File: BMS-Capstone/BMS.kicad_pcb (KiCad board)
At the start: 2 copper layers, 1 part, among them IC1 MP2634

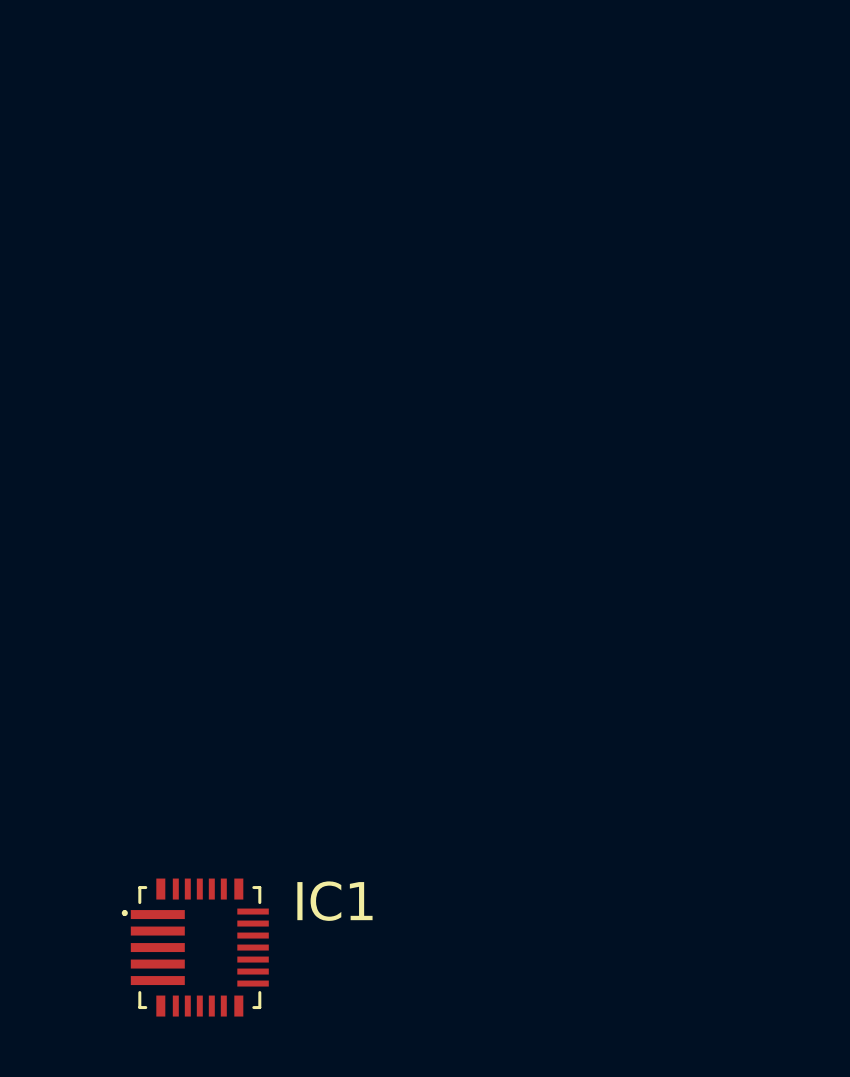
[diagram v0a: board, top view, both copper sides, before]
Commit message: Designed one entire MP chip layout
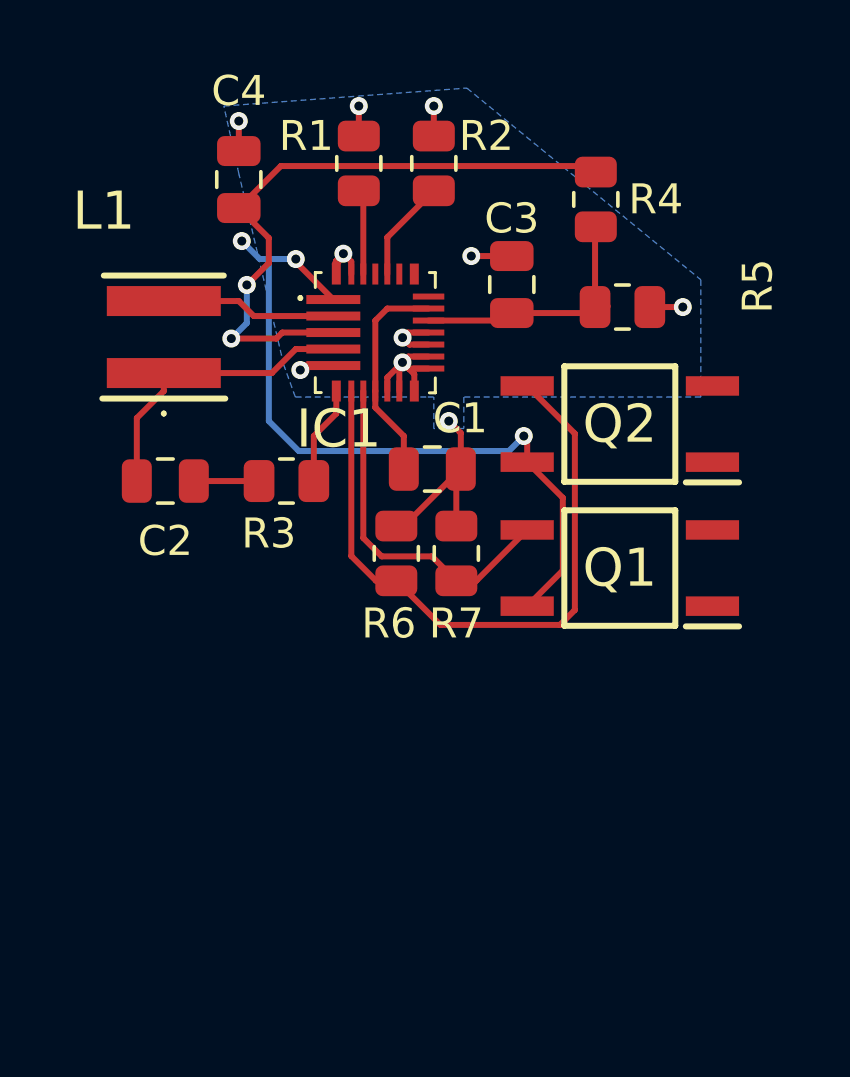
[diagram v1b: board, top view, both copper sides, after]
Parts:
- added C1: C, Capacitor_SMD:C_0805_2012Metric, F.Cu at (157.4, 79.1)
- added C2: C, Capacitor_SMD:C_0805_2012Metric, F.Cu at (148.6, 79.5)
- added C3: C, Capacitor_SMD:C_0805_2012Metric, F.Cu at (160.1, 73.0)
- added C4: C, Capacitor_SMD:C_0805_2012Metric, F.Cu at (151.0, 69.5)
- added L1: L, SamacSys_Parts:MPLAL4020R47 Inductor, F.Cu at (148.5, 74.7)
- added Q1: FODM121, SamacSys_Parts:SOP254P675X240-4N, F.Cu at (163.7, 82.4)
- added Q2: FODM121, SamacSys_Parts:SOP254P675X240-4N, F.Cu at (163.7, 77.6)
- added R1: R, Resistor_SMD:R_0805_2012Metric, F.Cu at (155.0, 68.9)
- added R2: R, Resistor_SMD:R_0805_2012Metric, F.Cu at (157.5, 68.9)
- added R3: 0, Resistor_SMD:R_0805_2012Metric, F.Cu at (152.6, 79.5)
- added R4: R, Resistor_SMD:R_0805_2012Metric, F.Cu at (162.9, 70.1)
- added R5: R, Resistor_SMD:R_0805_2012Metric, F.Cu at (163.8, 73.7)
- added R6: R, Resistor_SMD:R_0805_2012Metric, F.Cu at (156.2, 81.9)
- added R7: R, Resistor_SMD:R_0805_2012Metric, F.Cu at (158.2, 81.9)
- IC1: value MP2634 -> MP2643; footprint SamacSys_Parts:MP2634 -> SamacSys_Parts:MP2639AGRZ
- moved IC1 21.3 mm to (155.6, 74.5)
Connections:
- IC1 pad 1: unconnected-(IC1-CL-Pad1) -> /BMS Board/CELL1+/CELL2-
- IC1 pad 10: unconnected-(IC1-AGND-Pad10) -> /BMS Board/CELL1-
- IC1 pad 11: unconnected-(IC1-AGND-Pad11) -> /BMS Board/CELL1-
- IC1 pad 12: unconnected-(IC1-AGND-Pad12) -> /BMS Board/CELL1-
- IC1 pad 13: unconnected-(IC1-AGND-Pad13) -> /BMS Board/CELL1-
- IC1 pad 14: unconnected-(IC1-AGND-Pad14) -> /BMS Board/CELL1-
- IC1 pad 15: unconnected-(IC1-AGND-Pad15) -> /BMS Board/CELL1-
- IC1 pad 16: unconnected-(IC1-AGND-Pad16) -> /BMS Board/CELL1-
- IC1 pad 17: unconnected-(IC1-CU_FB-Pad17) -> Net-(IC1-CU_FB)
- IC1 pad 18: unconnected-(IC1-LOGIC-Pad18) -> /BMS Board/VCC1
- IC1 pad 2: unconnected-(IC1-LX-Pad2) -> Net-(IC1-LX)
- IC1 pad 22: unconnected-(IC1-LBC-Pad22) -> Net-(IC1-LBC)
- IC1 pad 23: unconnected-(IC1-AGND-Pad23) -> /BMS Board/CELL1-
- IC1 pad 24: unconnected-(IC1-UBC-Pad24) -> Net-(IC1-UBC)
- IC1 pad 25: unconnected-(IC1-AGND-Pad25) -> /BMS Board/CELL1-
- IC1 pad 26: unconnected-(IC1-AGND-Pad26) -> /BMS Board/CELL1-
- IC1 pad 3: unconnected-(IC1-CU-Pad3) -> /BMS Board/CELL2+/CELL3-
- IC1 pad 4: unconnected-(IC1-SW-Pad4) -> Net-(IC1-SW)
- IC1 pad 5: unconnected-(IC1-PGND-Pad5) -> /BMS Board/CELL1-
- IC1 pad 6: unconnected-(IC1-BST-Pad6) -> Net-(IC1-BST)
- IC1 pad 7: unconnected-(IC1-EN-Pad7) -> Net-(IC1-EN)
- IC1 pad 8: unconnected-(IC1-MODE-Pad8) -> Net-(IC1-MODE)
- IC1 pad 9: unconnected-(IC1-4V5-Pad9) -> /BMS Board/VCC1
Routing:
- net /BMS Board/CELL1+/CELL2-: track 0.00 -> 25.1 mm, vias 0 -> 3
- net Net-(IC1-EN): track 0.00 -> 22.2 mm
- net /BMS Board/CELL1-: track 0.00 -> 22.2 mm, vias 0 -> 10
- net /BMS Board/CELL2+/CELL3-: track 0.00 -> 21.7 mm, vias 0 -> 2
- net Net-(IC1-MODE): track 0.00 -> 11.9 mm
- net Net-(IC1-SW): track 0.00 -> 9.95 mm
- net Net-(IC1-CU_FB): track 0.00 -> 8.67 mm
- net /BMS Board/VCC1: track 0.00 -> 7.28 mm
- net Net-(IC1-LX): track 0.00 -> 5.86 mm
- net Net-(IC1-LBC): track 0.00 -> 3.42 mm
- net Net-(IC1-BST): track 0.00 -> 3.31 mm
- net Net-(IC1-UBC): track 0.00 -> 2.84 mm
- net Net-(C2-Pad1): track 0.00 -> 2.18 mm
- added copper zone on B.Cu, net /BMS Board/CELL1-

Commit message: Fixes
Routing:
- net /BMS Board/CELL1-: track 22.2 -> 24.9 mm, vias 10 -> 11
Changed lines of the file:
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@@
 		(tags "resistor")
 		(property "Reference" "R5"
-			(at 4.5125 -0.7 90)
+			(at 2.7125 -1.2 180)
 			(layer "F.SilkS")
 			(effects
@@
 	)
 	(segment
+		(start 155.55 72.6)
+		(end 155.55 70.834429)
+		(width 0.2)
+		(layer "F.Cu")
+		(net 5)
+	)
+	(segment
 		(start 160.1 72)
 		(end 158.75 72)
@@
 		(start 154.75 72.186915)
 		(end 154.484992 71.921907)
+		(width 0.2)
+		(layer "F.Cu")
+		(net 5)
+	)
+	(segment
+		(start 155.55 70.834429)
+		(end 156.226266 70.158163)
 		(width 0.2)
 		(layer "F.Cu")
@@
 		(net 5)
 	)
+	(via
+		(at 156.226266 70.158163)
+		(size 0.6)
+		(drill 0.3)
+		(layers "F.Cu" "B.Cu")
+		(free yes)
+		(net 5)
+	)

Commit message: More fixes
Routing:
- net /BMS Board/CELL1-: track 24.9 -> 23.0 mm
- net /BMS Board/CELL1+/CELL2-: track 25.1 -> 26.0 mm

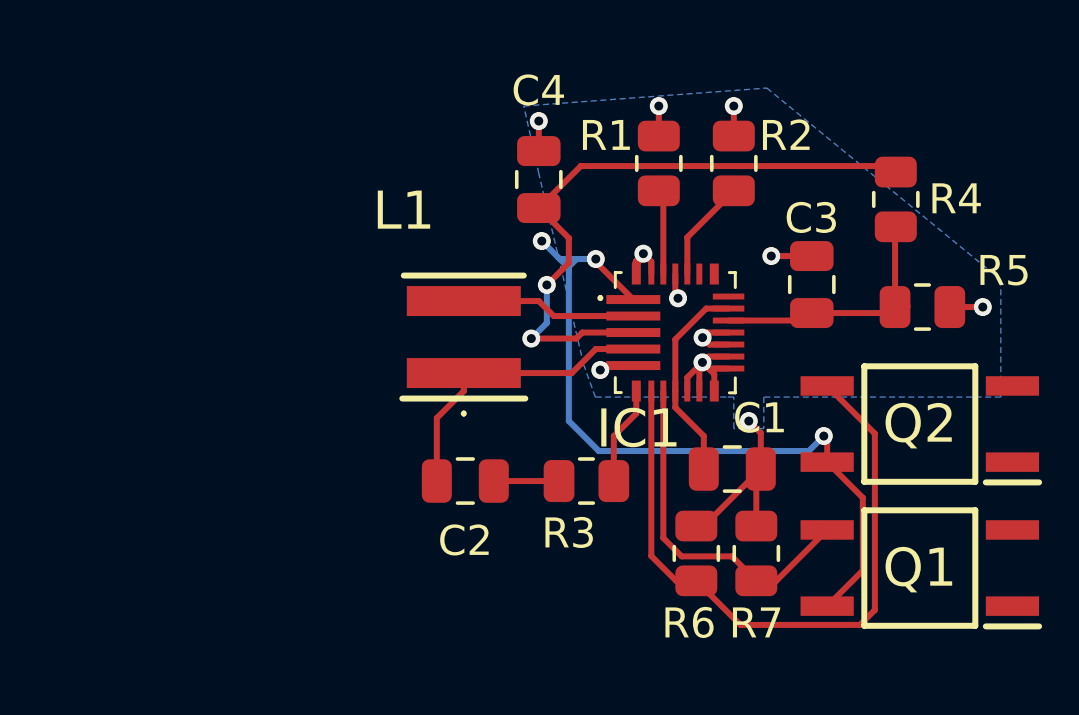
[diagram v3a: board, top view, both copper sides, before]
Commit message: added CL capacitor
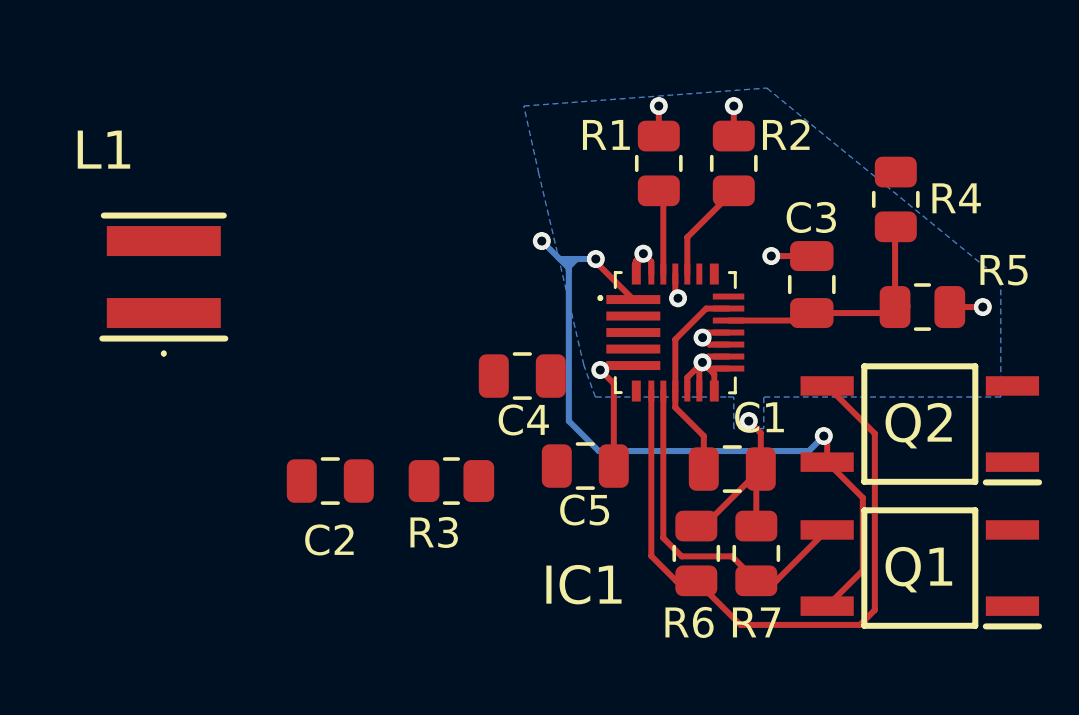
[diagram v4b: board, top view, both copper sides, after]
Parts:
- added C5: C, Capacitor_SMD:C_0805_2012Metric, F.Cu at (152.6, 79.0)
- moved L1 10.2 mm to (138.5, 72.7)
- moved C4 6.57 mm to (150.4, 76.0), turned to 0 degrees
- moved C2 4.50 mm to (144.1, 79.5)
- moved R3 4.50 mm to (148.1, 79.5)
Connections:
- net /BMS Board/CELL1+/CELL2- renamed /BMS Board/1Lower
- net /BMS Board/CELL1- renamed /BMS Board/1GND
- net /BMS Board/CELL2+/CELL3- renamed /BMS Board/1Upper
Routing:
- net /BMS Board/1Upper: track 21.7 -> 0.35 mm, vias 2 -> 0
- net Net-(IC1-SW): track 9.95 -> 0.00 mm
- net Net-(IC1-LX): track 5.86 -> 0.00 mm
- net Net-(IC1-BST): track 3.31 -> 0.00 mm
- net /BMS Board/1GND: track 23.0 -> 25.4 mm, vias 11 -> 10
- net Net-(C2-Pad1): track 2.18 -> 0.00 mm

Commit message: Redid the whole thing
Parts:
- moved R4 12.1 mm to (158.5, 81.4), turned to 90 degrees
- moved C3 7.78 mm to (156.5, 79.8), turned to 90 degrees
- moved L1 7.56 mm to (145.6, 75.3), turned to 0 degrees
- moved Q2 7.16 mm to (164.6, 84.7)
- moved R5 6.81 mm to (158.5, 78.0), turned to 90 degrees
- moved C2 5.69 mm to (148.0, 83.6), turned to 90 degrees
- moved C1 5.45 mm to (153.7, 83.0)
- moved IC1 5.29 mm to (152.1, 78.6)
- moved C4 5.27 mm to (147.2, 80.2), turned to -90 degrees
- moved C5 5.20 mm to (150.6, 74.2)
- moved R7 5.18 mm to (154.7, 85.7)
- moved R6 5.11 mm to (152.8, 85.7)
- moved R2 5.10 mm to (155.2, 73.5)
- moved R1 4.88 mm to (153.3, 73.5)
- moved R3 4.54 mm to (150.0, 83.6), turned to 90 degrees
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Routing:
- net /BMS Board/1GND: track 25.4 -> 3.39 mm, vias 10 -> 11
- net /BMS Board/1Upper: track 0.35 -> 15.5 mm, vias 0 -> 2
- net Net-(IC1-CU_FB): track 8.67 -> 0.00 mm
- net Net-(IC1-MODE): track 11.9 -> 20.0 mm
- net Net-(IC1-EN): track 22.2 -> 17.8 mm
- net /BMS Board/1Lower: track 26.0 -> 22.6 mm, vias 3 -> 4
- net Net-(IC1-BST): track 0.00 -> 2.50 mm
- net /BMS Board/VCC1: track 6.92 -> 8.83 mm, vias 0 -> 2
- net Net-(IC1-LBC): track 3.42 -> 3.92 mm
- net Net-(IC1-SW): track 0.00 -> 0.09 mm, vias 0 -> 9

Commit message: Slight modifications
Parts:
- added C10: C, Capacitor_SMD:C_0805_2012Metric, F.Cu at (150.1, 94.7)
- added C6: C, Capacitor_SMD:C_0805_2012Metric, F.Cu at (156.0, 100.3)
- added C7: C, Capacitor_SMD:C_0805_2012Metric, F.Cu at (146.7, 100.7)
- added C8: C, Capacitor_SMD:C_0805_2012Metric, F.Cu at (153.2, 103.5)
- added C9: C, Capacitor_SMD:C_0805_2012Metric, F.Cu at (147.5, 104.1)
- added IC2: MP2643, SamacSys_Parts:MP2639AGRZ, F.Cu at (151.6, 99.1)
- added L2: L, SamacSys_Parts:MPLAL4020R47 Inductor, F.Cu at (145.1, 95.8)
- added Q3: FODM121, SamacSys_Parts:SOP254P675X240-4N, F.Cu at (164.1, 100.5)
- added Q4: FODM121, SamacSys_Parts:SOP254P675X240-4N, F.Cu at (164.1, 105.2)
- added R10: 0, Resistor_SMD:R_0805_2012Metric, F.Cu at (154.7, 94.0)
- added R11: R, Resistor_SMD:R_0805_2012Metric, F.Cu at (152.8, 94.0)
- added R12: R, Resistor_SMD:R_0805_2012Metric, F.Cu at (149.5, 104.1)
- added R13: R, Resistor_SMD:R_0805_2012Metric, F.Cu at (152.3, 106.2)
- added R14: R, Resistor_SMD:R_0805_2012Metric, F.Cu at (154.2, 106.2)
- added R8: R, Resistor_SMD:R_0805_2012Metric, F.Cu at (158.0, 101.9)
- added R9: R, Resistor_SMD:R_0805_2012Metric, F.Cu at (158.0, 98.5)
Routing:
- net /BMS Board/1Upper: track 15.5 -> 41.3 mm, vias 2 -> 6
- net Net-(IC2-MODE): track 0.00 -> 20.0 mm
- net Net-(IC2-EN): track 0.00 -> 17.8 mm
- net /BMS Board/2Upper: track 0.00 -> 17.5 mm, vias 0 -> 2
- net /BMS Board/VCC2: track 0.00 -> 8.83 mm, vias 0 -> 2
- net /BMS Board/1Lower: track 22.6 -> 30.3 mm, vias 4 -> 15
- net Net-(IC2-LBC): track 0.00 -> 3.92 mm
- net Net-(IC2-UBC): track 0.00 -> 3.10 mm
- net /BMS Board/1GND: track 3.39 -> 6.48 mm
- net Net-(IC2-CU_FB): track 0.00 -> 2.87 mm
- net Net-(IC1-CU_FB): track 0.00 -> 2.87 mm
- net Net-(IC2-BST): track 0.00 -> 2.50 mm
- net Net-(IC2-SW): track 0.00 -> 0.09 mm, vias 0 -> 9
- added copper zone on B.Cu, net /BMS Board/1Lower
- removed copper zone on B.Cu, net /BMS Board/1GND
